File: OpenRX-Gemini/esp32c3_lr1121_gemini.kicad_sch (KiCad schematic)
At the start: 67 parts, among them T1 0900PC16J0042001E, T2 0900PC16J0042001E, U1 ESP32-C3FH4, U10 RFX2401C, U11 SKY13588-460LF, U2 TLV75533PDQNR, U3 TS2306A 240GF MSM 9_C2976675, U4 LR1121IMLTRT, U5 OW7EL89CENUYO3YLC-32M, U6 SKY13588-460LF, U7 RFX2401C, U8 OW7EL89CENUYO3YLC-32M, U9 LR1121IMLTRT, X1 CJ17-400001010B20

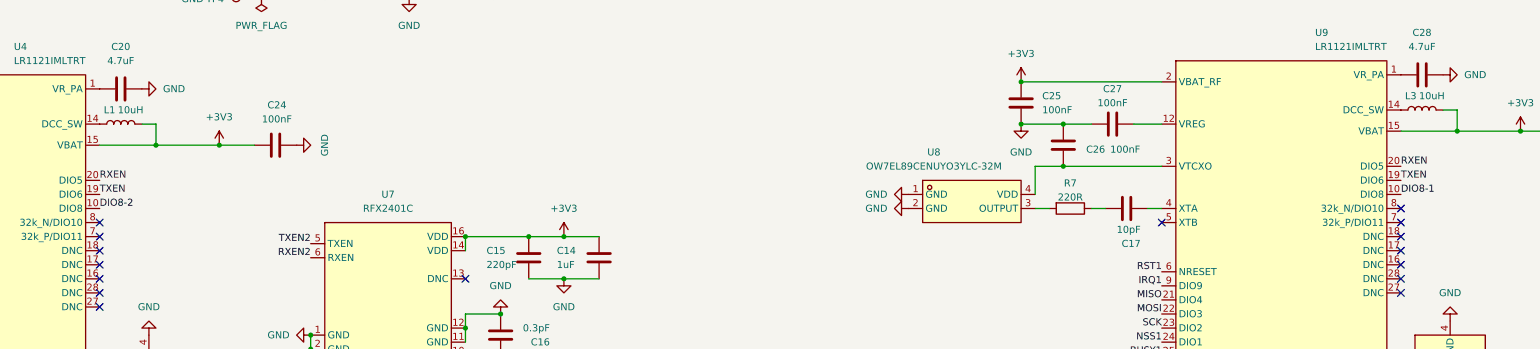
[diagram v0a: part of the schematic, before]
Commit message: Repo cleanup: final state for handoff
- Clean README with architecture, BOM, CE notes, status
- Remove dated analysis files (absorbed into FINAL_NETLIST + KICAD_WORKFLOW)
- Remove stale OpenRX-Dual (archived), ERC reports, backups, prl files
- Updated .gitignore for .kicad_dru, production backups
- CERN-OHL-S v2 license confirmed
- 3 active projects: Lite, Mono, Gemini
- Schematics final, initial PCB layouts done, routing in progress
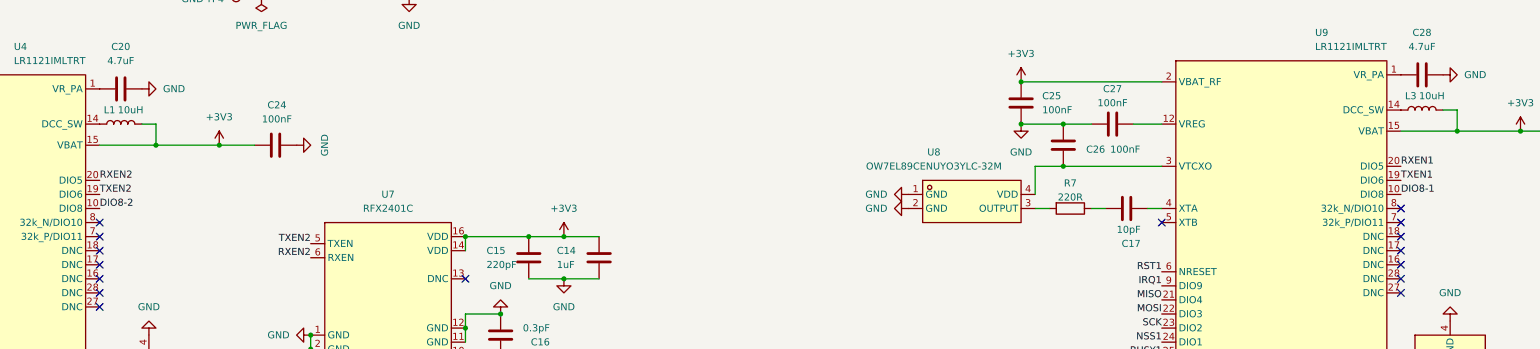
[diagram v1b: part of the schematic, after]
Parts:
- C16, C30: LCSC (none) -> C76927
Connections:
- net RXEN1: now also U9.20 (DIO5)
- net RXEN2: now also U4.20 (DIO5)
- net TXEN1: now also U9.19 (DIO6)
- net TXEN2: now also U4.19 (DIO6)
- removed net RXEN: U4.20 (DIO5), U9.20 (DIO5)
- removed net TXEN: U4.19 (DIO6), U9.19 (DIO6)
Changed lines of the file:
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@@
 		)
 	)
-	(label "RXEN"
+	(label "RXEN1"
 		(at 365.76 152.4 0)
 		(effects
@@
 		)
 	)
-	(label "TXEN"
+	(label "TXEN1"
 		(at 365.76 154.94 0)
 		(effects
@@
 		)
 	)
-	(label "TXEN"
+	(label "TXEN2"
 		(at 130.81 157.48 0)
 		(effects
@@
 		)
 	)
-	(label "RXEN"
+	(label "RXEN2"
 		(at 130.81 154.94 0)
 		(effects
@@
 			)
 		)
-		(property "LCSC" ""
+		(property "LCSC" "C76927"
 			(at 648.97 297.18 0)
 			(hide yes)
@@
 			)
 		)
-		(property "LCSC" ""
+		(property "LCSC" "C76927"
 			(at 414.02 299.72 0)
 			(hide yes)
